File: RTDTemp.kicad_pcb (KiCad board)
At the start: 2 copper layers, 90 x 70 mm, 91 parts, among them J1 Conn_01x02, J11 Conn_01x02, J4 CAN_In, J5 CAN_Out, U2 Nucleo_L432KC, U3 PDS1-Sx-Sx, U5 ADM3055E, U7 CDSOT23-T24CAN

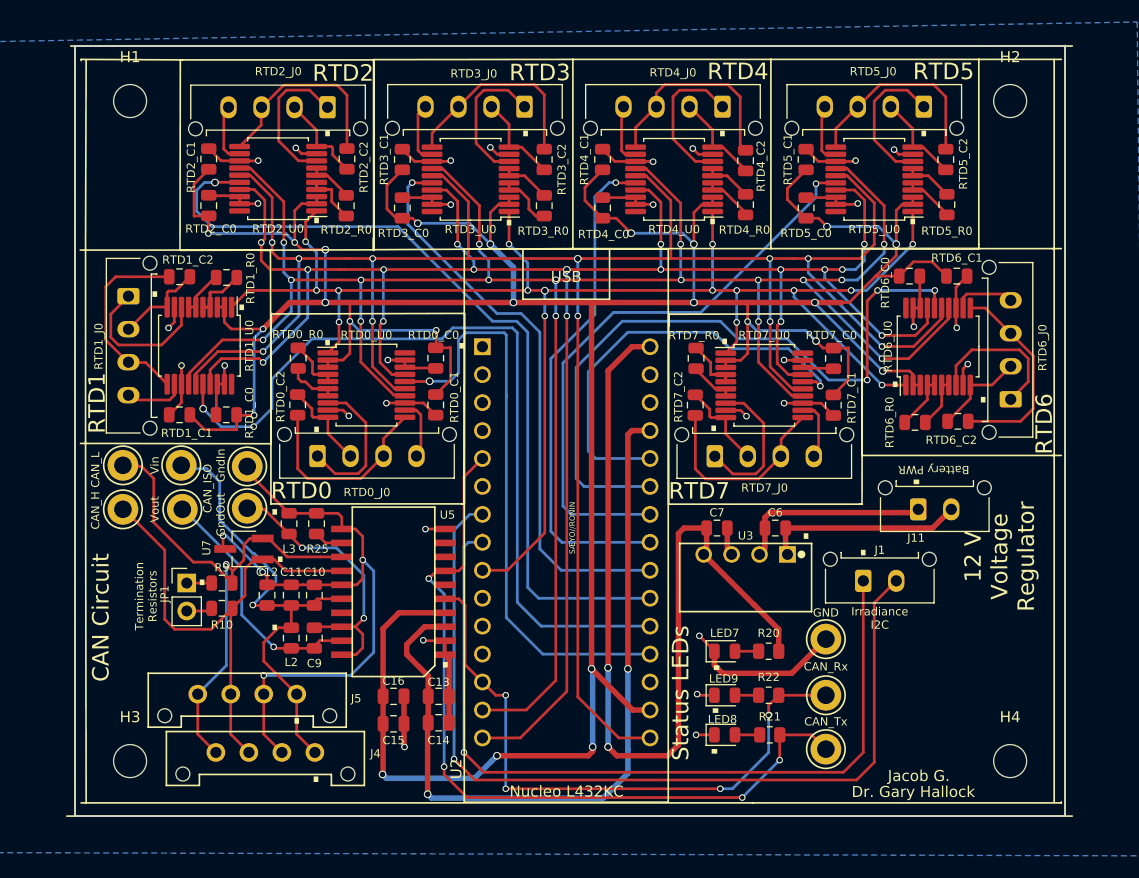
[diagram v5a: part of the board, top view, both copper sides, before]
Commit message: cleanup of edge silkscreen and slight component reposition
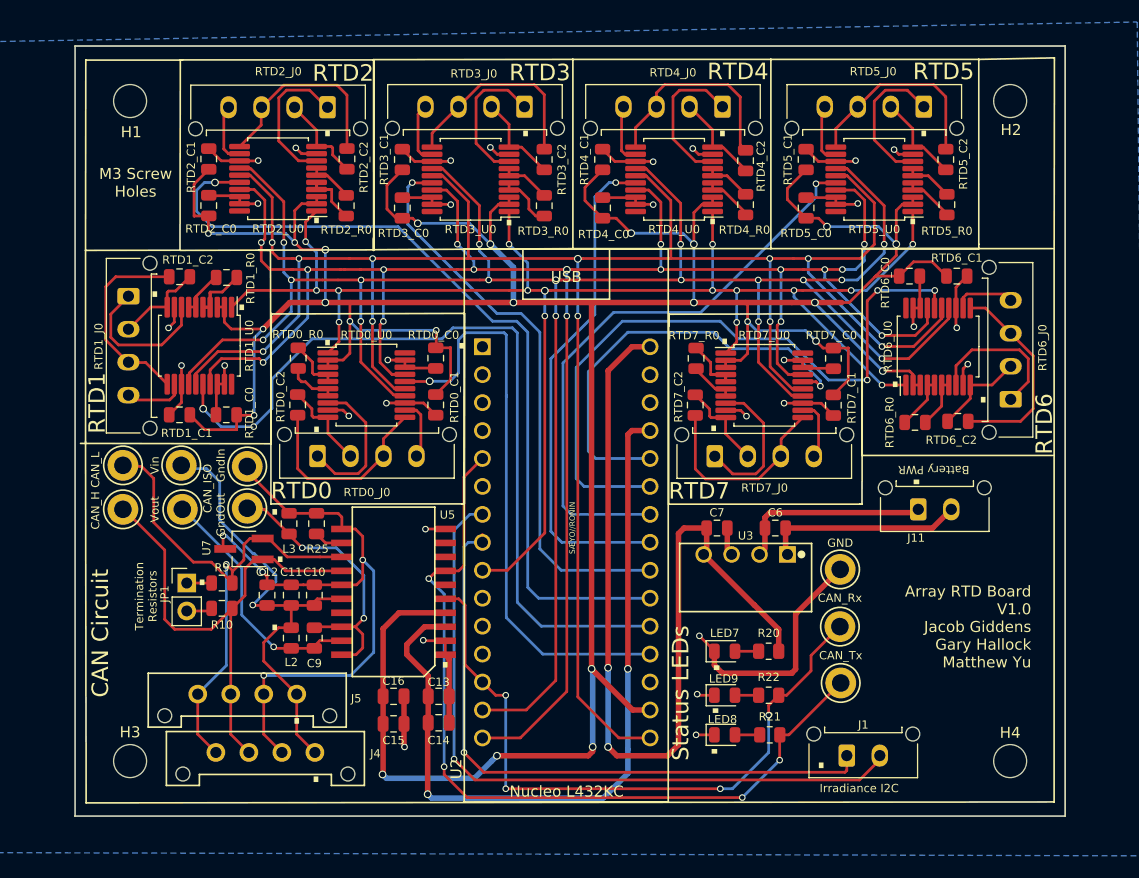
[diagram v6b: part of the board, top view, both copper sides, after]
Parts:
- moved J1 16.0 mm to (167.1, 83.7)
- moved GND 6.47 mm to (166.4, 66.8)
- moved CAN_Rx 6.37 mm to (166.4, 72.0)
- moved CAN_Tx 6.16 mm to (166.5, 77.1)
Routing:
- net Net-(J1-Pad1): track 74.5 -> 58.1 mm
- net Net-(J1-Pad2): track 81.0 -> 64.6 mm
- net GND: track 134.1 -> 141.0 mm
- net /CAN_Rx: track 55.9 -> 60.6 mm
- net /CAN_Tx: track 73.0 -> 75.8 mm
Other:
- board text added: "Array RTD Board V1.0 Jacob Giddens Gary Hallock Matthew Yu"
- board text added: "M3 Screw Holes"
- board text removed: "12 V Voltage Regulator"
- board text removed: "Dr. Gary Hallock"
- board text removed: "Jacob G."

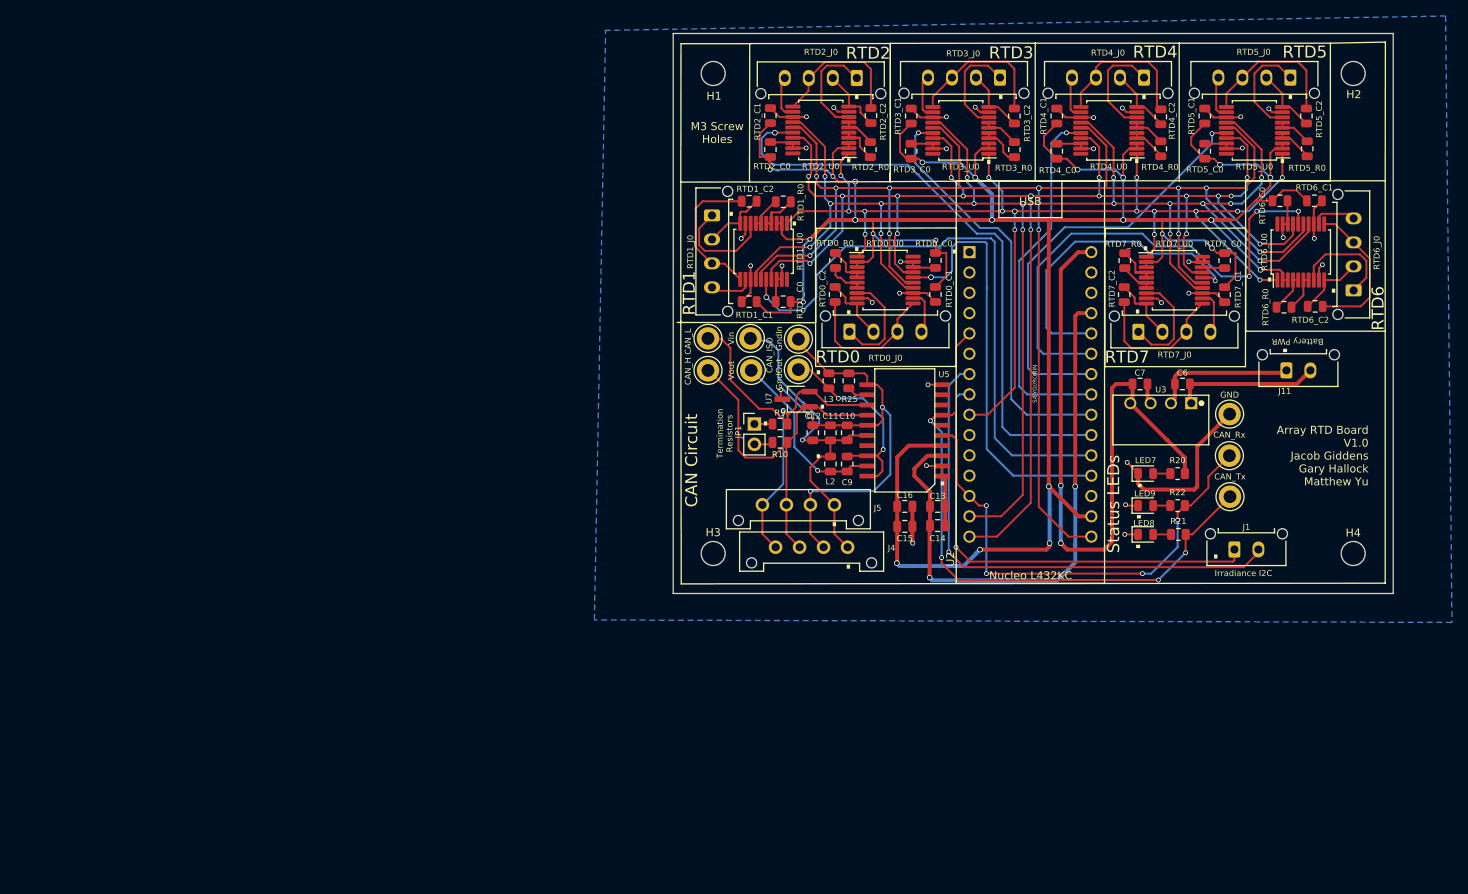
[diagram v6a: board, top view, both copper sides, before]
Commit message: PR ready RTD/Irradiance Sensor Board. Added extra mounts for irradiance I2C and updated power reg to match MPPT. Also cleaner layout.
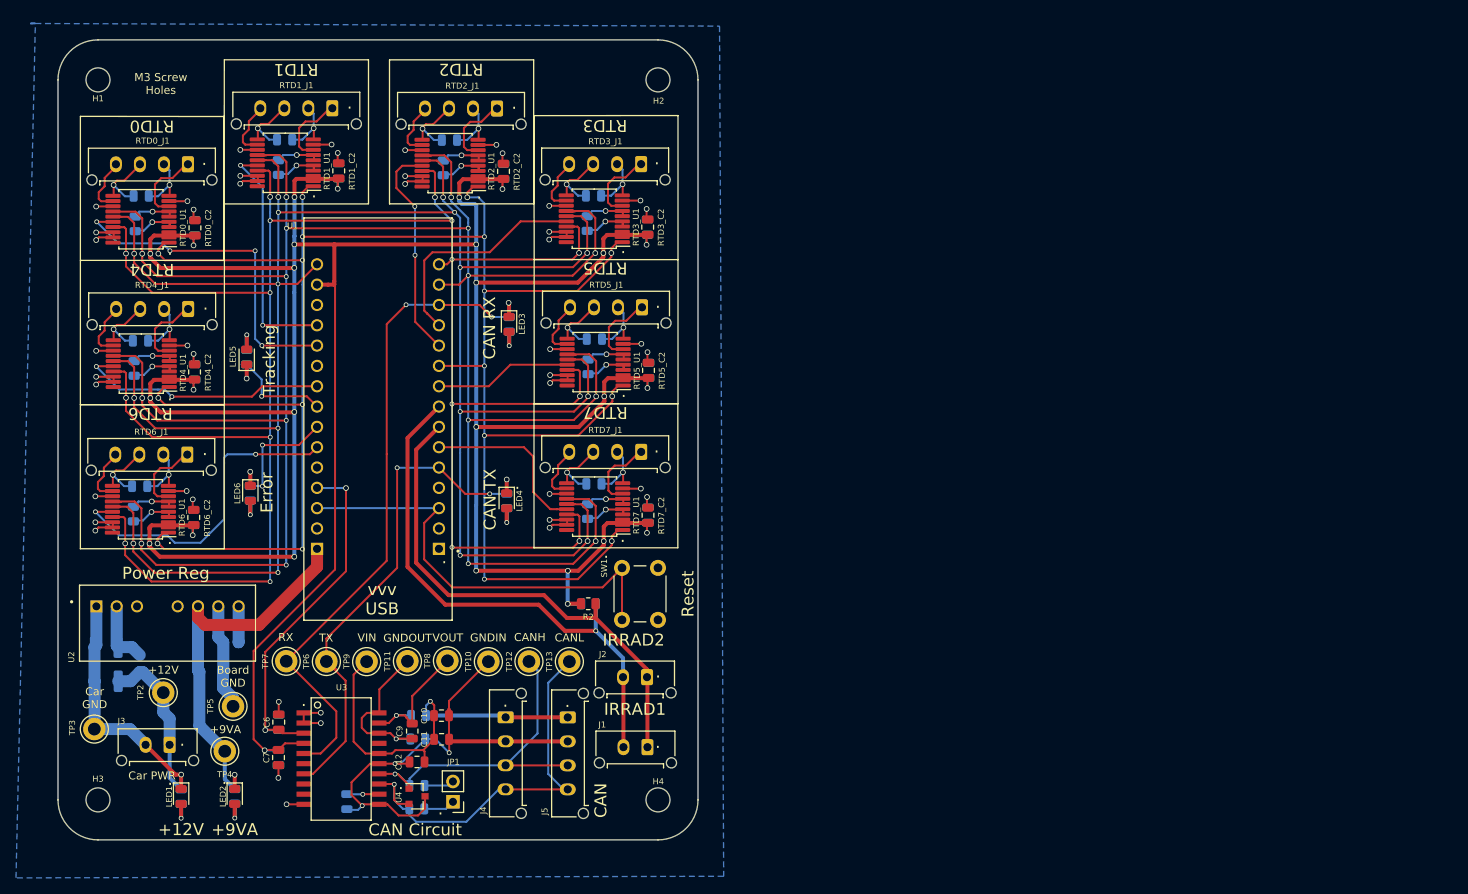
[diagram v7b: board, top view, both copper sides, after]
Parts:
- removed the C10 at (118.7, 69.1)
- removed the C6 at (160.6, 63.0)
- removed the C7 at (155.2, 63.0)
- removed CAN_Rx: CAN_Rx, TestPoint:TestPoint_Keystone_5005-5009_Compact
- removed GND: GND, TestPoint:TestPoint_Keystone_5005-5009_Compact
- removed J11: Conn_01x02, Connector_Molex:Molex_Micro-Fit_3.0_43650-0215_1x02_P3.00mm_Vertical
- removed RTD0_C0, RTD1_C0, RTD2_C0, RTD3_C0, RTD4_C0, RTD5_C0, RTD6_C0, RTD7_C0: 100nF, Capacitor_SMD:C_0805_2012Metric
- removed RTD0_J0, RTD1_J0, RTD2_J0, RTD3_J0, RTD4_J0, RTD5_J0, RTD6_J0, RTD7_J0: Conn_01x04, Connector_Molex:Molex_Micro-Fit_3.0_43650-0415_1x04_P3.00mm_Vertical
- removed RTD0_R0, RTD1_R0, RTD2_R0, RTD3_R0, RTD4_R0, RTD5_R0, RTD6_R0, RTD7_R0: 400, Resistor_SMD:R_0805_2012Metric
- removed RTD0_U0, RTD1_U0, RTD2_U0, RTD3_U0, RTD4_U0, RTD5_U0, RTD6_U0, RTD7_U0: MAX31865xAP, Package_SO:SSOP-20_5.3x7.2mm_P0.65mm
- removed the U3 at (157.8, 65.4)
- added C1: 100uF, Capacitor_SMD:C_1210_3225Metric, B.Cu at (26.1, 100.2)
- added C2: 47uF, Capacitor_SMD:C_1210_3225Metric, B.Cu at (26.0, 95.9)
- added C3: 10uF, Capacitor_SMD:C_0805_2012Metric, B.Cu at (41.6, 95.3)
- added C4: 100uF, Capacitor_SMD:C_1210_3225Metric, B.Cu at (39.1, 99.0)
- added C9: 0.22uF, Capacitor_SMD:C_0805_2012Metric, F.Cu at (64.3, 106.4)
- added G***: LOGO, UTSVT_Special:UTSVT_Logo_Symbol, B.Cu at (60.5, 45.1)
- added G***: LOGO, UTSVT_Special:Hallock_Image, B.Cu at (60.9, 76.1)
- added J2: Conn_01x02, Connector_Molex:Molex_Micro-Fit_3.0_43650-0215_1x02_P3.00mm_Vertical, F.Cu at (93.6, 99.7)
- added J3: Car Power, Connector_Molex:Molex_Micro-Fit_3.0_43650-0215_1x02_P3.00mm_Vertical, F.Cu at (34.0, 108.1)
- added L1: 4.7uH, Inductor_SMD:L_0805_2012Metric, B.Cu at (30.2, 98.0)
- added LED1: Car Power Live (Green), LED_SMD:LED_0805_2012Metric, F.Cu at (35.4, 114.6)
- added LED5: Tracking (Blue), LED_SMD:LED_0805_2012Metric, F.Cu at (43.6, 59.6)
- added LED6: Error (Amber), LED_SMD:LED_0805_2012Metric, F.Cu at (44.0, 76.7)
- added R1: 4.7k, Resistor_SMD:R_0805_2012Metric, B.Cu at (86.3, 90.5)
- added R2: 4.7k, Resistor_SMD:R_0805_2012Metric, F.Cu at (86.3, 90.5)
- added R3: 1.5K, Resistor_SMD:R_0805_2012Metric, B.Cu at (35.4, 114.6)
- added R7: 330, Resistor_SMD:R_0805_2012Metric, B.Cu at (43.6, 59.7)
- added R8: 330, Resistor_SMD:R_0805_2012Metric, B.Cu at (44.0, 76.7)
- added RTD0_C3: 100nF, Capacitor_SMD:C_0805_2012Metric, B.Cu at (30.4, 39.5)
- added RTD0_J1: Conn_01x04, Connector_Molex:Molex_Micro-Fit_3.0_43650-0415_1x04_P3.00mm_Vertical, F.Cu at (36.2, 35.5)
- added RTD0_R1: 400, Resistor_SMD:R_0805_2012Metric, B.Cu at (29.6, 43.0)
- added RTD0_U1: MAX31865xAP, Package_SO:SSOP-20_5.3x7.2mm_P0.65mm, F.Cu at (30.4, 42.4)
- added RTD1_C3: 100nF, Capacitor_SMD:C_0805_2012Metric, B.Cu at (48.3, 32.5)
- added RTD1_J1: Conn_01x04, Connector_Molex:Molex_Micro-Fit_3.0_43650-0415_1x04_P3.00mm_Vertical, F.Cu at (54.3, 28.6)
- added RTD1_R1: 400, Resistor_SMD:R_0805_2012Metric, B.Cu at (47.5, 36.0)
- added RTD1_U1: MAX31865xAP, Package_SO:SSOP-20_5.3x7.2mm_P0.65mm, F.Cu at (48.4, 35.4)
- added RTD2_C3: 100nF, Capacitor_SMD:C_0805_2012Metric, B.Cu at (68.9, 32.5)
- added RTD2_J1: Conn_01x04, Connector_Molex:Molex_Micro-Fit_3.0_43650-0415_1x04_P3.00mm_Vertical, F.Cu at (74.9, 28.6)
- added RTD2_R1: 400, Resistor_SMD:R_0805_2012Metric, B.Cu at (68.2, 36.0)
- added RTD2_U1: MAX31865xAP, Package_SO:SSOP-20_5.3x7.2mm_P0.65mm, F.Cu at (69.0, 35.4)
- added RTD3_C3: 100nF, Capacitor_SMD:C_0805_2012Metric, B.Cu at (86.9, 39.5)
- added RTD3_J1: Conn_01x04, Connector_Molex:Molex_Micro-Fit_3.0_43650-0415_1x04_P3.00mm_Vertical, F.Cu at (92.9, 35.5)
- added RTD3_R1: 400, Resistor_SMD:R_0805_2012Metric, B.Cu at (86.2, 43.0)
- added RTD3_U1: MAX31865xAP, Package_SO:SSOP-20_5.3x7.2mm_P0.65mm, F.Cu at (87.0, 42.4)
- added RTD4_C3: 100nF, Capacitor_SMD:C_0805_2012Metric, B.Cu at (30.3, 57.6)
- added RTD4_J1: Conn_01x04, Connector_Molex:Molex_Micro-Fit_3.0_43650-0415_1x04_P3.00mm_Vertical, F.Cu at (36.3, 53.6)
- added RTD4_R1: 400, Resistor_SMD:R_0805_2012Metric, B.Cu at (29.5, 61.1)
- added RTD4_U1: MAX31865xAP, Package_SO:SSOP-20_5.3x7.2mm_P0.65mm, F.Cu at (30.4, 60.5)
- added RTD5_C3: 100nF, Capacitor_SMD:C_0805_2012Metric, B.Cu at (87.0, 57.4)
- added RTD5_J1: Conn_01x04, Connector_Molex:Molex_Micro-Fit_3.0_43650-0415_1x04_P3.00mm_Vertical, F.Cu at (93.0, 53.4)
- added RTD5_R1: 400, Resistor_SMD:R_0805_2012Metric, B.Cu at (86.3, 60.9)
- added RTD5_U1: MAX31865xAP, Package_SO:SSOP-20_5.3x7.2mm_P0.65mm, F.Cu at (87.1, 60.3)
- added RTD6_C3: 100nF, Capacitor_SMD:C_0805_2012Metric, B.Cu at (30.2, 75.8)
- added RTD6_J1: Conn_01x04, Connector_Molex:Molex_Micro-Fit_3.0_43650-0415_1x04_P3.00mm_Vertical, F.Cu at (36.2, 71.8)
- added RTD6_R1: 400, Resistor_SMD:R_0805_2012Metric, B.Cu at (29.4, 79.3)
- added RTD6_U1: MAX31865xAP, Package_SO:SSOP-20_5.3x7.2mm_P0.65mm, F.Cu at (30.3, 78.7)
- added RTD7_C3: 100nF, Capacitor_SMD:C_0805_2012Metric, B.Cu at (87.0, 75.5)
- added RTD7_J1: Conn_01x04, Connector_Molex:Molex_Micro-Fit_3.0_43650-0415_1x04_P3.00mm_Vertical, F.Cu at (92.9, 71.5)
- added RTD7_R1: 400, Resistor_SMD:R_0805_2012Metric, B.Cu at (86.2, 79.0)
- added RTD7_U1: MAX31865xAP, Package_SO:SSOP-20_5.3x7.2mm_P0.65mm, F.Cu at (87.1, 78.3)
- added SW1: SW_Push, Button_Switch_THT:SW_PUSH_6mm, F.Cu at (90.5, 92.5)
- added TP2: Car +12V, TestPoint:TestPoint_Keystone_5005-5009_Compact, F.Cu at (33.2, 101.6)
- added TP3: Car GND, TestPoint:TestPoint_Keystone_5005-5009_Compact, F.Cu at (24.5, 106.2)
- added TP4: +9VA, TestPoint:TestPoint_Keystone_5005-5009_Compact, F.Cu at (40.9, 108.9)
- added TP5: GNDP, TestPoint:TestPoint_Keystone_5005-5009_Compact, F.Cu at (41.9, 103.3)
- added TP7: CAN_Rx, TestPoint:TestPoint_Keystone_5005-5009_Compact, F.Cu at (48.5, 97.7)
- added U1: Nucleo_L432KC, Array-RTDPCB:MODULE_NUCLEO-L432KC, F.Cu at (60.0, 67.4)
- C10: renamed from C9; value 10u -> 10uF
- C11: value 0.1u -> 0.01uF
- C12: value 0.01u -> 0.1uF
- C5: renamed from C13; value 10u -> 10uF; moved to B.Cu
- C6: renamed from C14; value 0.1u -> 0.1uF
- C7: renamed from C15; value 0.1u -> 0.1uF
- C8: renamed from C16; value 0.01u -> 0.01uF; moved to B.Cu
- J4, J5: footprint UTSVT_Connectors:Molex_MicroFit3.0_1x4xP3.00mm_PolarizingPeg_Vertical -> Connector_Molex:Molex_Micro-Fit_3.0_43650-0415_1x04_P3.00mm_Vertical
- L2, L3: value 2k -> 1.8kH; moved to B.Cu
- LED2: renamed from LED7; value Iso 9V Live? -> Device 9V Live (Green)
- LED3: renamed from LED9; value CAN_Rx -> CAN_Rx (Blue)
- LED4: renamed from LED8; value CAN_Tx -> CAN_Tx (Blue)
- R10, RTD0_C1, RTD1_C1, RTD2_C1, RTD3_C1, RTD4_C1, RTD5_C1, RTD6_C1, RTD7_C1: moved to B.Cu
- R11: renamed from R9; moved to B.Cu
- R4: renamed from R20; value 1K -> 1.1K; moved to B.Cu
- R5: renamed from R22; value 330R -> 330; moved to B.Cu
- R6: renamed from R21; value 330R -> 330; moved to B.Cu
- R9: renamed from R25; moved to B.Cu
- U2: value Nucleo_L432KC -> PWR_REG_PQMC3-Dx-Sx-S; footprint UTSVT_Special:NucleoL432KC -> Array-RTDPCB:490_PQMC3_D12_S12_S
- U3: renamed from U5; footprint UTSVT_ICs:SOIC-20W_7.5x15.4mm_Pitch1.27mm -> Array-RTDPCB:ADM3055EBRIZ
- U4: renamed from U7; footprint Package_TO_SOT_SMD:SOT-23W_Handsoldering -> Package_TO_SOT_SMD:SOT-23
- moved RTD6_C1 145.6 mm to (37.0, 79.7), turned to 90 degrees
- moved RTD6_C2 142.6 mm to (37.0, 79.7), turned to 90 degrees
- moved RTD4_C2 124.9 mm to (37.1, 61.5)
- moved R4 124.6 mm to (42.1, 114.6), turned to 90 degrees
- moved LED2 120.8 mm to (42.1, 114.6), turned to 270 degrees
- moved TP6 114.8 mm to (53.5, 97.7), turned to 90 degrees
- moved RTD4_C1 112.4 mm to (37.1, 61.5)
- moved U2 111.6 mm to (33.7, 92.9), turned to 0 degrees
- moved RTD0_C1 92.9 mm to (37.1, 43.5), turned to 90 degrees
- moved H4 92.2 mm to (95.0, 115.0)
- moved RTD5_C2 88.2 mm to (93.8, 61.3)
- moved H2 86.9 mm to (95.0, 25.0)
- moved C5 86.7 mm to (47.6, 105.3), turned to 90 degrees
- moved R5 86.6 mm to (76.4, 55.6), turned to 90 degrees
- moved C6 85.9 mm to (47.6, 105.3), turned to 90 degrees
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- renumbered TP15 to TP10, TP16 to TP11, TP21 to TP12, TP22 to TP13, CAN_Tx to TP6, TP13 to TP8, TP14 to TP9
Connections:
- C10 pad 1: Net-(C9-Pad1) -> Net-(C10-Pad1)
- C10 pad 2: Net-(C9-Pad2) -> Net-(C10-Pad2)
- C5 pad 2: GND -> GNDPWR
- C6 pad 2: GND -> GNDPWR
- C7 pad 2: GND -> GNDPWR
- C8 pad 2: GND -> GNDPWR
- LED2 pad 1: GND -> GNDPWR
- LED3 pad 1: GND -> GNDPWR
- LED4 pad 1: GND -> GNDPWR
- RTD0_C1 pad 2: GND -> GNDPWR
- RTD0_C2 pad 1: Net-(RTD0_C2-Pad1) -> +3V3
- RTD0_C2 pad 2: Net-(RTD0_C2-Pad2) -> GNDPWR
- RTD1_C1 pad 2: GND -> GNDPWR
- RTD1_C2 pad 1: Net-(RTD1_C2-Pad1) -> +3V3
- RTD1_C2 pad 2: Net-(RTD1_C2-Pad2) -> GNDPWR
- RTD2_C1 pad 2: GND -> GNDPWR
- RTD2_C2 pad 1: Net-(RTD2_C2-Pad1) -> +3V3
- RTD2_C2 pad 2: Net-(RTD2_C2-Pad2) -> GNDPWR
- RTD3_C1 pad 2: GND -> GNDPWR
- RTD3_C2 pad 1: Net-(RTD3_C2-Pad1) -> +3V3
- RTD3_C2 pad 2: Net-(RTD3_C2-Pad2) -> GNDPWR
- RTD4_C1 pad 2: GND -> GNDPWR
- RTD4_C2 pad 1: Net-(RTD4_C2-Pad1) -> +3V3
- RTD4_C2 pad 2: Net-(RTD4_C2-Pad2) -> GNDPWR
- RTD5_C1 pad 2: GND -> GNDPWR
- RTD5_C2 pad 1: Net-(RTD5_C2-Pad1) -> +3V3
- RTD5_C2 pad 2: Net-(RTD5_C2-Pad2) -> GNDPWR
- RTD6_C1 pad 2: GND -> GNDPWR
- RTD6_C2 pad 1: Net-(RTD6_C2-Pad1) -> +3V3
- RTD6_C2 pad 2: Net-(RTD6_C2-Pad2) -> GNDPWR
- RTD7_C1 pad 2: GND -> GNDPWR
- RTD7_C2 pad 1: Net-(RTD7_C2-Pad1) -> +3V3
- RTD7_C2 pad 2: Net-(RTD7_C2-Pad2) -> GNDPWR
- U2 pad 1: Net-(U2-Pad1) -> GNDREF
- U2 pad 5: /CAN_Tx -> Net-(U2-Pad5)
- U2 pad 6: Net-(U2-Pad6) -> +9VA
- U2 pad 7: Net-(J1-Pad2) -> GNDPWR
- U2 pad 8: Net-(J1-Pad1) -> Net-(C3-Pad2)
- U3 pad 1: GND -> GNDPWR
- U3 pad 10: GND -> GNDPWR
- U3 pad 2: GND -> GNDPWR
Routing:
- net /SDI: track 0.00 -> 302.0 mm, vias 0 -> 16
- net /CLK: track 0.00 -> 293.2 mm, vias 0 -> 16
- net /SDO: track 0.00 -> 274.7 mm, vias 0 -> 16
- net /DRDY: track 0.00 -> 250.3 mm, vias 0 -> 17
- net SDI: track 206.8 -> 0.00 mm, vias 17 -> 0
- net CLK: track 202.6 -> 0.00 mm, vias 11 -> 0
- net SDO: track 196.2 -> 0.00 mm, vias 17 -> 0
- net DRDY: track 145.9 -> 0.00 mm, vias 16 -> 0
- net GND: track 141.0 -> 0.00 mm, vias 30 -> 0
- net GNDPWR: track 18.0 -> 120.2 mm, vias 0 -> 50
- net CS_2: track 75.5 -> 0.00 mm, vias 1 -> 0
- net CS_1: track 74.4 -> 0.00 mm, vias 2 -> 0
- net CS_6: track 62.9 -> 0.00 mm, vias 3 -> 0
- net /Reset: track 0.00 -> 56.1 mm
- net +3V3: track 340.3 -> 396.2 mm, vias 24 -> 27
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- added copper zone on B.Cu, net GNDPWR
- removed copper zone on B.Cu, net GND
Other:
- board size 90 x 70 mm -> 80 x 100 mm
- board text added: "+12V"
- board text added: "+3V3"
- board text added: "+9VA"
- board text added: "Board GND"
- board text added: "CAN"
- board text added: "CAN RX"
- board text added: "CAN TX"
- board text added: "CANH"
- board text added: "CANL"
- board text added: "CLK"
- board text added: "Car GND"
- board text added: "Car PWR"
- board text added: "DRDY"
- board text added: "Error"
- board text added: "GNDIN"
- board text added: "GNDOUT"
- board text added: "IRRAD1"
- board text added: "IRRAD2"
- board text added: "Power Reg"
- board text added: "RX"
- board text added: "Reset"
- board text added: "SDI"
- board text added: "SDO"
- board text added: "TX"
- board text added: "Tracking"
- board text added: "VIN"
- board text added: "VOUT"
- board text added: "vvv USB"
- board text removed: "Battery PWR"
- board text removed: "CAN_H"
- board text removed: "CAN_ISO"
- board text removed: "CAN_L"
- board text removed: "CLK SDO SDI DRDY V3.3"
- board text removed: "GndIn"
- board text removed: "GndOut"
- board text removed: "Irradiance I2C"
- board text removed: "Status LEDs"
- board text removed: "SÆYO//RONIN"
- board text removed: "Termination Resistors"
- board text removed: "Vin"
- board text removed: "Vout"

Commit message: Addressed review.
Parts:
- TP5: value GNDP -> Device GND
- moved G*** 1.34 mm to (60.6, 43.8)
- moved G*** 0.62 mm to (60.5, 76.6)
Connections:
- C1 pad 2: GNDREF -> GNDPWR
- C2 pad 2: GNDREF -> GNDPWR
- C3 pad 1: GNDPWR -> GNDREF
- C4 pad 2: GNDPWR -> GNDREF
- C5 pad 2: GNDPWR -> GNDREF
- C6 pad 2: GNDPWR -> GNDREF
- C7 pad 2: GNDPWR -> GNDREF
- C8 pad 2: GNDPWR -> GNDREF
- J3 pad 2: GNDREF -> GNDPWR
- LED1 pad 1: GNDREF -> GNDPWR
- LED2 pad 1: GNDPWR -> GNDREF
- LED3 pad 1: GNDPWR -> GNDREF
- LED4 pad 1: GNDPWR -> GNDREF
- LED5 pad 1: GNDPWR -> GNDREF
- LED6 pad 1: GNDPWR -> GNDREF
- RTD0_C1 pad 2: GNDPWR -> GNDREF
- RTD0_C2 pad 2: GNDPWR -> GNDREF
- RTD0_U1 pad 13: GNDPWR -> GNDREF
- RTD0_U1 pad 18: GNDPWR -> GNDREF
- RTD0_U1 pad 19: GNDPWR -> GNDREF
- RTD0_U1 pad 9: GNDPWR -> GNDREF
- RTD1_C1 pad 2: GNDPWR -> GNDREF
- RTD1_C2 pad 2: GNDPWR -> GNDREF
- RTD1_U1 pad 13: GNDPWR -> GNDREF
- RTD1_U1 pad 18: GNDPWR -> GNDREF
- RTD1_U1 pad 19: GNDPWR -> GNDREF
- RTD1_U1 pad 9: GNDPWR -> GNDREF
- RTD2_C1 pad 2: GNDPWR -> GNDREF
- RTD2_C2 pad 2: GNDPWR -> GNDREF
- RTD2_U1 pad 13: GNDPWR -> GNDREF
- RTD2_U1 pad 18: GNDPWR -> GNDREF
- RTD2_U1 pad 19: GNDPWR -> GNDREF
- RTD2_U1 pad 9: GNDPWR -> GNDREF
- RTD3_C1 pad 2: GNDPWR -> GNDREF
- RTD3_C2 pad 2: GNDPWR -> GNDREF
- RTD3_U1 pad 13: GNDPWR -> GNDREF
- RTD3_U1 pad 18: GNDPWR -> GNDREF
- RTD3_U1 pad 19: GNDPWR -> GNDREF
- RTD3_U1 pad 9: GNDPWR -> GNDREF
- RTD4_C1 pad 2: GNDPWR -> GNDREF
- RTD4_C2 pad 2: GNDPWR -> GNDREF
- RTD4_U1 pad 13: GNDPWR -> GNDREF
- RTD4_U1 pad 18: GNDPWR -> GNDREF
- RTD4_U1 pad 19: GNDPWR -> GNDREF
- RTD4_U1 pad 9: GNDPWR -> GNDREF
- RTD5_C1 pad 2: GNDPWR -> GNDREF
- RTD5_C2 pad 2: GNDPWR -> GNDREF
- RTD5_U1 pad 13: GNDPWR -> GNDREF
- RTD5_U1 pad 18: GNDPWR -> GNDREF
- RTD5_U1 pad 19: GNDPWR -> GNDREF
- RTD5_U1 pad 9: GNDPWR -> GNDREF
- RTD6_C1 pad 2: GNDPWR -> GNDREF
- RTD6_C2 pad 2: GNDPWR -> GNDREF
- RTD6_U1 pad 13: GNDPWR -> GNDREF
- RTD6_U1 pad 18: GNDPWR -> GNDREF
- RTD6_U1 pad 19: GNDPWR -> GNDREF
- RTD6_U1 pad 9: GNDPWR -> GNDREF
- RTD7_C1 pad 2: GNDPWR -> GNDREF
- RTD7_C2 pad 2: GNDPWR -> GNDREF
- RTD7_U1 pad 13: GNDPWR -> GNDREF
- RTD7_U1 pad 18: GNDPWR -> GNDREF
- RTD7_U1 pad 19: GNDPWR -> GNDREF
- RTD7_U1 pad 9: GNDPWR -> GNDREF
- SW1 pad 2: GNDPWR -> GNDREF
- TP3 pad 1: GNDREF -> GNDPWR
- TP5 pad 1: GNDPWR -> GNDREF
- U1 pad 29: GNDPWR -> GNDREF
- U1 pad 4: GNDPWR -> GNDREF
- U2 pad 1: GNDREF -> GNDPWR
- U2 pad 7: GNDPWR -> GNDREF
- U3 pad 1: GNDPWR -> GNDREF
- U3 pad 10: GNDPWR -> GNDREF
- U3 pad 2: GNDPWR -> GNDREF
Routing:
- net GNDREF: track 30.7 -> 120.2 mm, vias 1 -> 50
- net GNDPWR: track 120.2 -> 30.7 mm, vias 50 -> 1
- added copper zone on B.Cu, net GNDREF
- removed copper zone on B.Cu, net GNDPWR
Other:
- board text added: "UTSVT - Array RTD/Irradiance Sensor Board v1.0 Fall 2020 Jacob Giddens Gary Hallock Matthew Yu"
- board text removed: "Array RTD Board V1.0 Jacob Giddens Gary Hallock Matthew Yu"
